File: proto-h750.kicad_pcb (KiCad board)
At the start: 2 copper layers, 158 parts, among them J1 Conn_02x08_Odd_Even, J10 Conn_02x02_Odd_Even, J11 Conn_02x02_Odd_Even, J12 Conn_01x02, J13 Conn_01x02, J2 USB_B_Micro, J3 Conn_02x02_Odd_Even, J4 Conn_02x14_Odd_Even, J5 Conn_02x08_Odd_Even, J6 AudioJack3, J7 Conn_02x02_Odd_Even, J8 Screw_Terminal_01x02, J9 AudioJack3, Q1 BS170, Q2 BS170, Q3 BS170, Q4 IRF540N, Q5 BSS138, Q6 MMBT2222, SW1 SW_DIP_x01, SW2 SW_DIP_x01, SW3 SW_DIP_x01, T1 Transformer_1P_1S, U1 STA516BETR, U10 BGA2869, U11 BGA2869, U2 STM32H750VBT6, U3 AP1117-33, U4 LM7805_TO220, U5 LM7812_TO220, U6 LM5134AMF_NOPB, U9 SA612, X1 ASV-xxxMHz, Y1 16MHz, Y2 ECS-10.7-7.5B

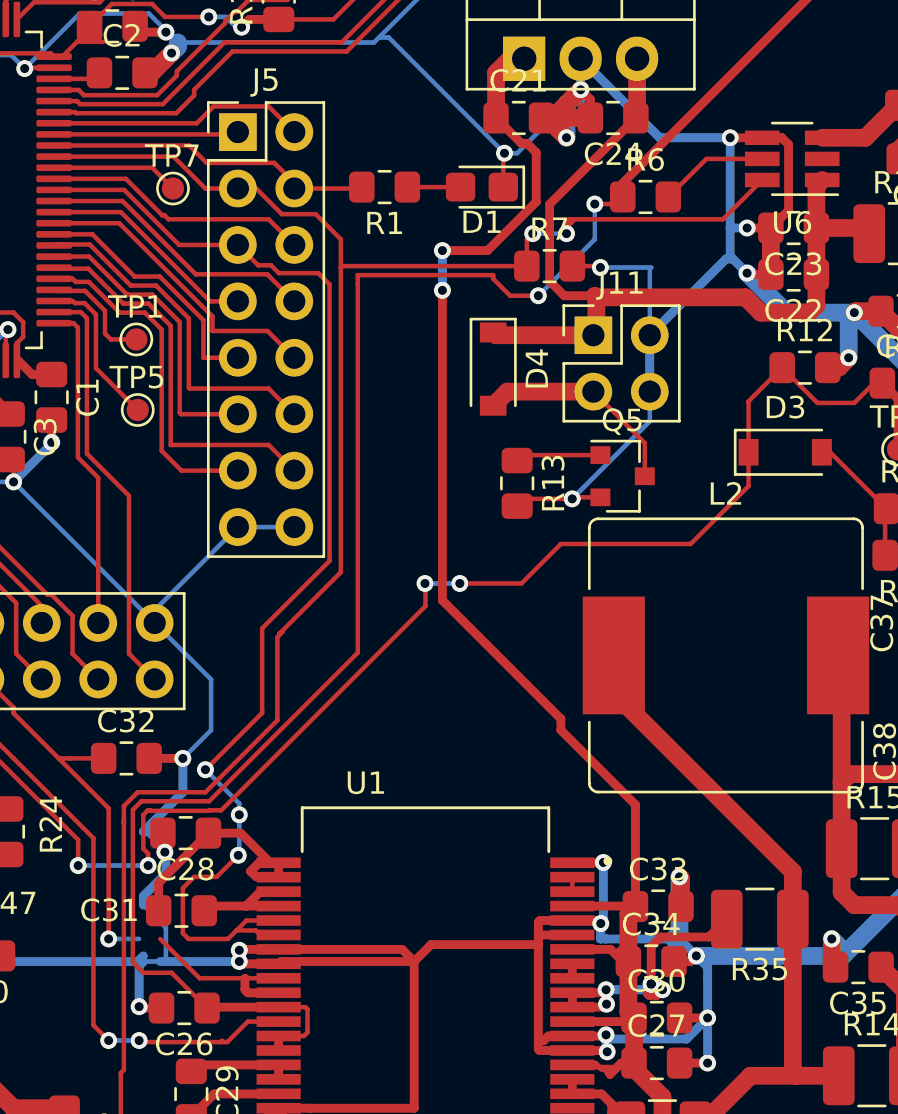
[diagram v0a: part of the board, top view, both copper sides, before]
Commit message: All tracks routed
DRC to be cleared
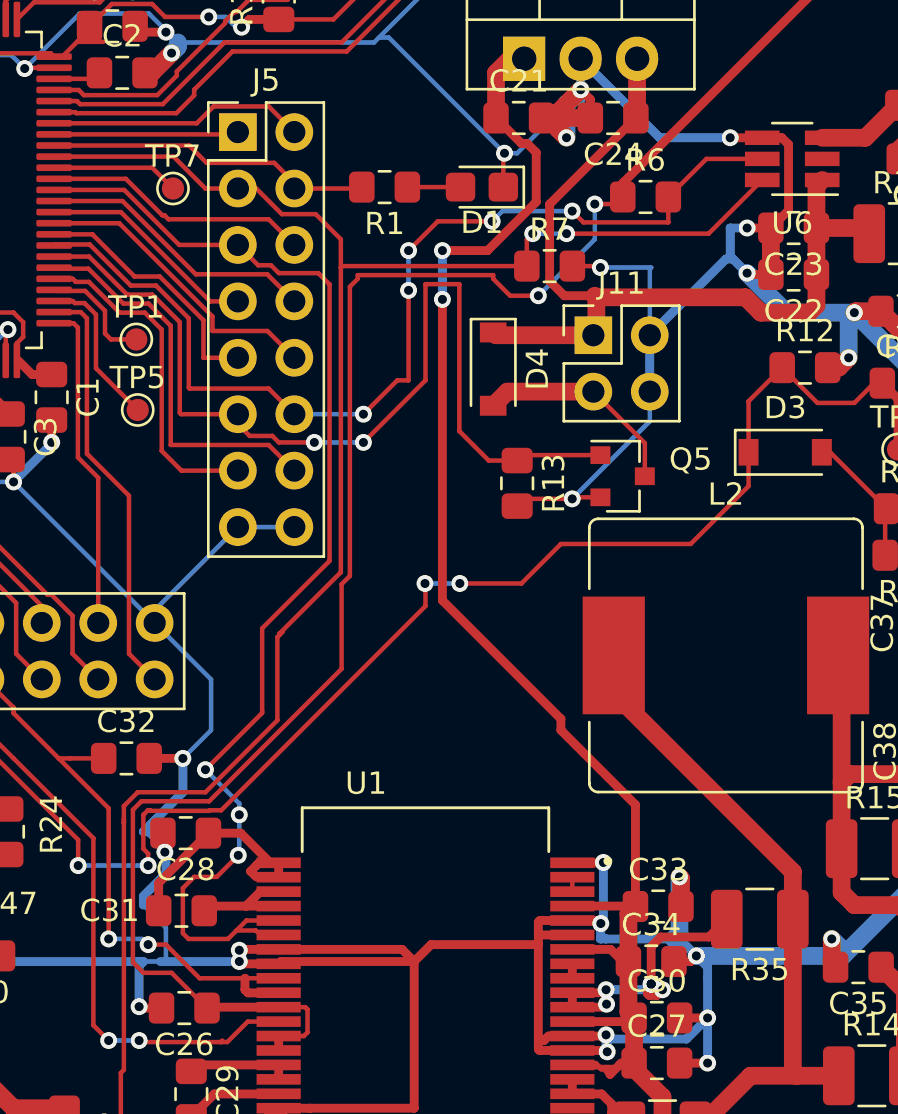
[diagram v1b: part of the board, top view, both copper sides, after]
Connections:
- J4 pad 10: TX_ENA -> /PE2
- J4 pad 12: RXTX -> /PE0
- J5 pad 11: /PD10 -> RXTX
- J5 pad 12: /PD11 -> TX_ENA
- U2 pad 1: TX_ENA -> /PE2
- U2 pad 57: /PD10 -> RXTX
- U2 pad 58: /PD11 -> TX_ENA
- U2 pad 97: RXTX -> /PE0
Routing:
- net RXTX: track 15.8 -> 43.5 mm, vias 0 -> 2
- net TX_ENA: track 24.4 -> 46.2 mm, vias 2 -> 5
- net /PE2: track 0.00 -> 19.4 mm, vias 0 -> 2
- net /PD11: track 15.8 -> 0.00 mm
- net /PD10: track 13.6 -> 0.00 mm
- net /PE0: track 0.00 -> 12.0 mm
- net GND: track 960.5 -> 956.1 mm
- net +24V: track 103.7 -> 104.8 mm
- net A_FAULT: track 40.8 -> 41.7 mm, vias 1 -> 2
- net MCO: track 102.9 -> 102.1 mm

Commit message: DRC OK
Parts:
- moved TP13 1.14 mm to (104.1, 86.1)
- moved TP15 0.90 mm to (106.2, 86.9)
- moved R38 0.76 mm to (106.4, 90.4)
- moved C40 0.51 mm to (128.8, 121.9)
- moved R17 0.51 mm to (128.8, 125.0)
- moved X1 0.25 mm to (98.0, 84.3)
- moved C5 0.25 mm to (103.9, 76.2)
- moved L1 0.25 mm to (100.6, 68.1)
- moved C14 0.25 mm to (103.9, 78.2)
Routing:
- net GND: track 956.1 -> 962.5 mm
- net Net-(C5-Pad2): track 12.1 -> 13.4 mm
- net /PA2: track 9.71 -> 10.7 mm
- net /nRESET: track 138.5 -> 139.3 mm
- net /PA0: track 9.08 -> 9.89 mm
- net (no net): track 0.80 -> 0.00 mm
- net Net-(R35-Pad2): track 14.0 -> 13.3 mm
- net Net-(C31-Pad2): track 5.18 -> 5.83 mm
- net A_PWM: track 54.7 -> 55.4 mm
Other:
- copper layers 2 -> 4
- net class Default: clearance 0.2032 -> 0.127; trace_width 0.2032 -> 0.127; via_dia 0.762 -> 0.6; via_drill 0.4064 -> 0.3
- rule pad_to_mask_clearance: 0.0508 -> 0
- rule solder_mask_min_width: 0.1524 -> 0.12
- rule trace_clearance: 0.2032 -> 0.127
- rule trace_min: 0.2032 -> 0.127
- rule via_min_drill: 0.3048 -> 0.3
- rule via_min_size: 0.4064 -> 0.6

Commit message: DRC OK 2
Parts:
- moved R35 5.00 mm to (150.6, 110.0)
- moved C34 2.03 mm to (150.1, 107.4)
- moved C33 1.62 mm to (150.1, 105.4)
- moved C30 0.51 mm to (150.4, 112.5)
- moved C27 0.51 mm to (150.4, 114.6)
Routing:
- net +24V: track 104.8 -> 122.5 mm
- net Net-(R35-Pad2): track 13.3 -> 6.30 mm, vias 5 -> 0
- net Net-(L2-Pad1): track 30.5 -> 36.5 mm
- net GND: track 962.5 -> 964.1 mm

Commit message: Some pouring
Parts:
- added C60: 100n, Capacitor_SMD:C_0805_2012Metric_Pad1.15x1.40mm_HandSolder, F.Cu at (93.2, 84.1)
- added H5: MountingHole_Pad, MountingHole:MountingHole_3.2mm_M3_Pad_Via, F.Cu at (140.0, 110.6)
- T1: footprint Transformer_THT:Transformer_Toroid_Horizontal_D10.5mm_Amidon-T37 -> Transformer_THT:Transformer_Toroid_Horizontal_D14.0mm_Amidon-T50
- moved J12 5.80 mm to (134.6, 135.1)
- moved R17 5.08 mm to (133.3, 127.3), turned to 270 degrees
- moved C40 4.76 mm to (133.3, 123.2), turned to 270 degrees
- moved T1 3.88 mm to (128.0, 135.6)
- moved R5 2.60 mm to (123.2, 114.6)
- moved C29 0.40 mm to (129.5, 115.1)
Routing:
- net Net-(J10-Pad1): track 45.9 -> 79.6 mm
- net Net-(L2-Pad1): track 36.5 -> 67.3 mm
- net MODUL_OUT: track 35.7 -> 65.4 mm
- net VCC_CPU: track 183.9 -> 209.3 mm
- net GND: track 964.1 -> 976.3 mm, vias 93 -> 140
- net Net-(T1-Pad3): track 9.50 -> 18.3 mm
- net Net-(C41-Pad1): track 11.3 -> 15.4 mm
- net Net-(C20-Pad1): track 26.7 -> 30.4 mm
- net Net-(C40-Pad1): track 3.32 -> 6.67 mm
- net Net-(C46-Pad1): track 4.67 -> 6.77 mm
- net MCO: track 102.1 -> 100.0 mm
- net Net-(C40-Pad2): track 4.02 -> 2.01 mm
- net +5V: track 314.5 -> 313.0 mm
- net Net-(C42-Pad1): track 7.41 -> 7.94 mm
- added copper zone on F.Cu, net +24V
- added copper zone on F.Cu, net GND
- added copper zone on F.Cu, net VCC
- added copper zone on F.Cu, net VCC_CPU

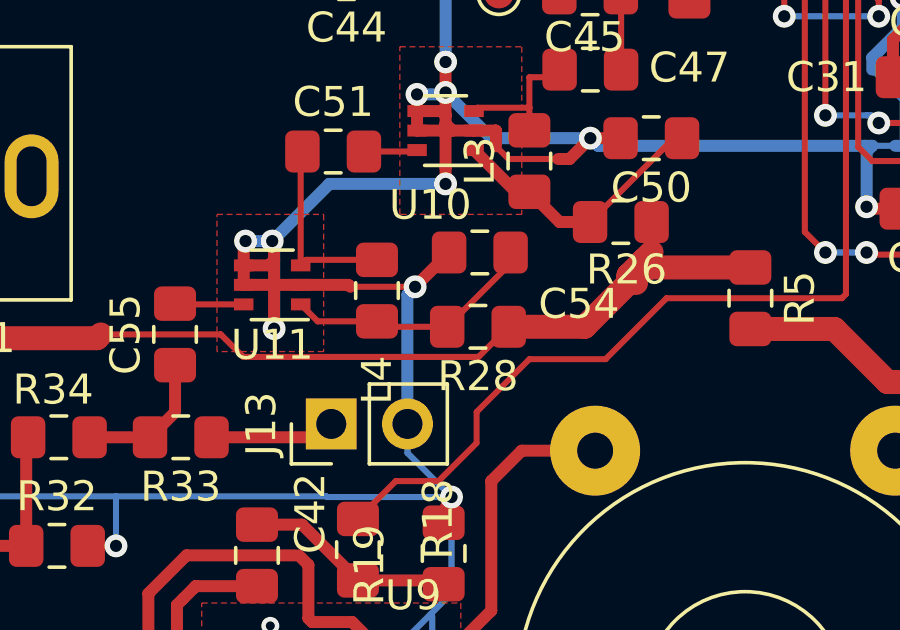
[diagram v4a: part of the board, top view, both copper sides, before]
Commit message: Better MMIC DC link
To be done on other
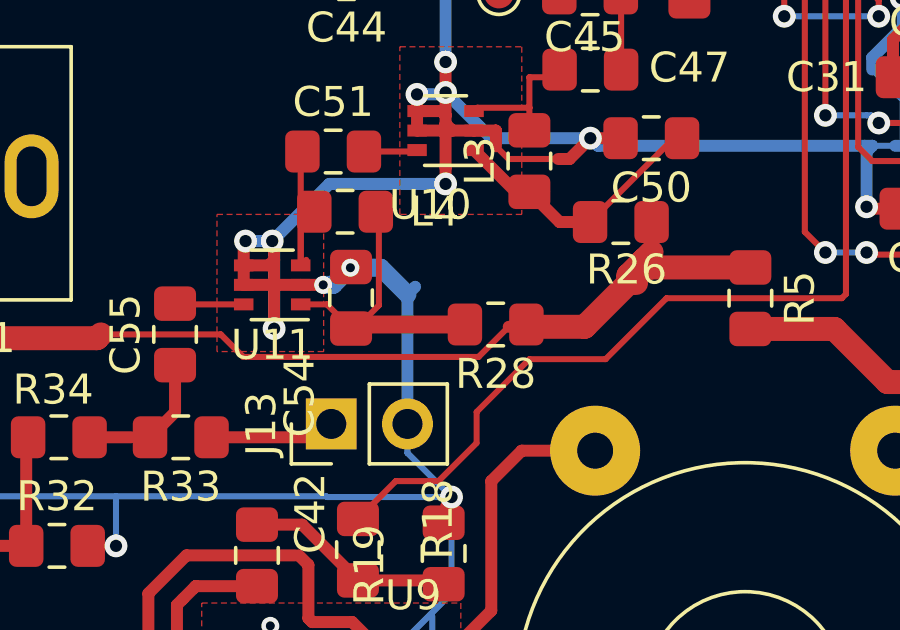
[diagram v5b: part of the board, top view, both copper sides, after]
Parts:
- moved C54 4.55 mm to (109.9, 114.5), turned to 90 degrees
- moved L4 2.84 mm to (109.7, 111.7), turned to 180 degrees
- moved R28 0.60 mm to (114.7, 115.4)
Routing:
- net Net-(C54-Pad1): track 8.54 -> 10.3 mm
- net GND: track 976.3 -> 975.0 mm, vias 140 -> 141
